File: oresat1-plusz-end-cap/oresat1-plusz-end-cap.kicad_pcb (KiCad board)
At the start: 4 copper layers, 105.6 x 105.6 mm, 48 parts, among them J1 M55-7011242R, J2 U.FL-R-SMA, U1 RM3100, U2 RM3100

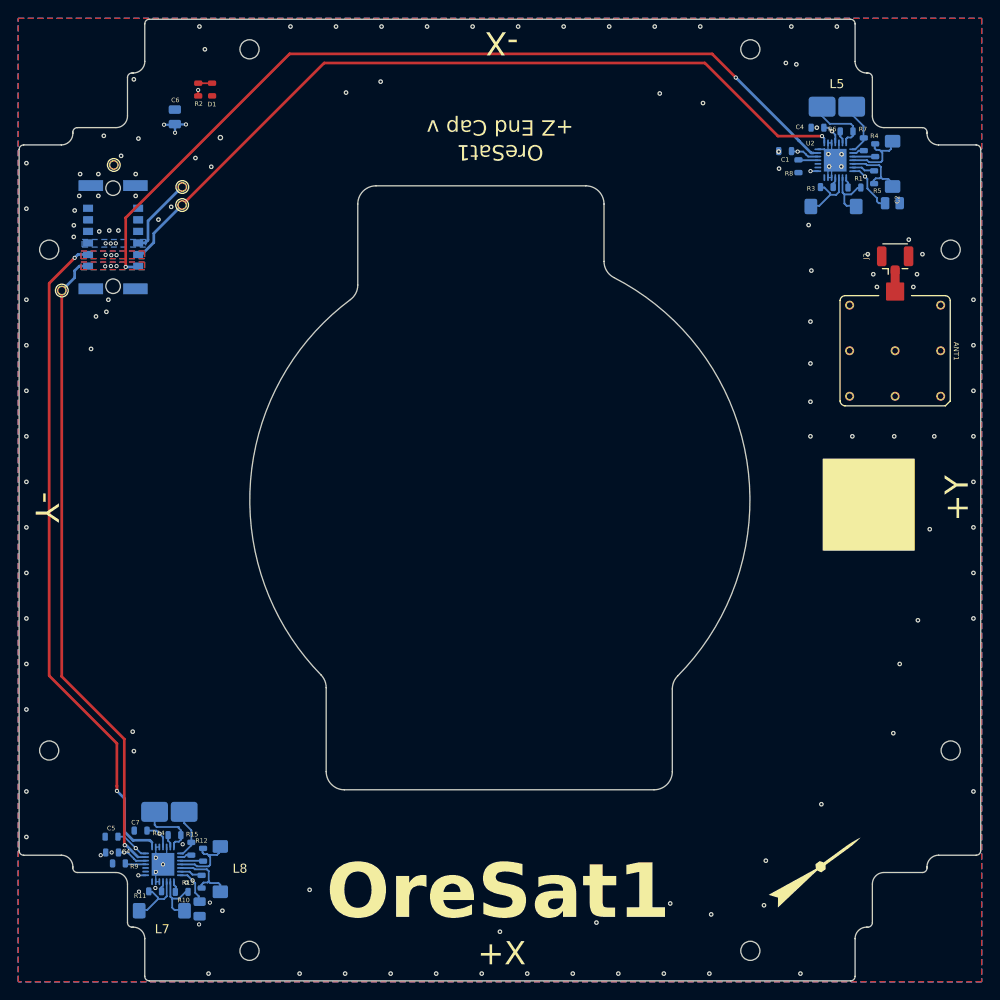
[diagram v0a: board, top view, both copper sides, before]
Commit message: Added 3D models and fixed fab des
3D models of antenna patch (-Z) and M55 connector & magIc2 chip on both boards.
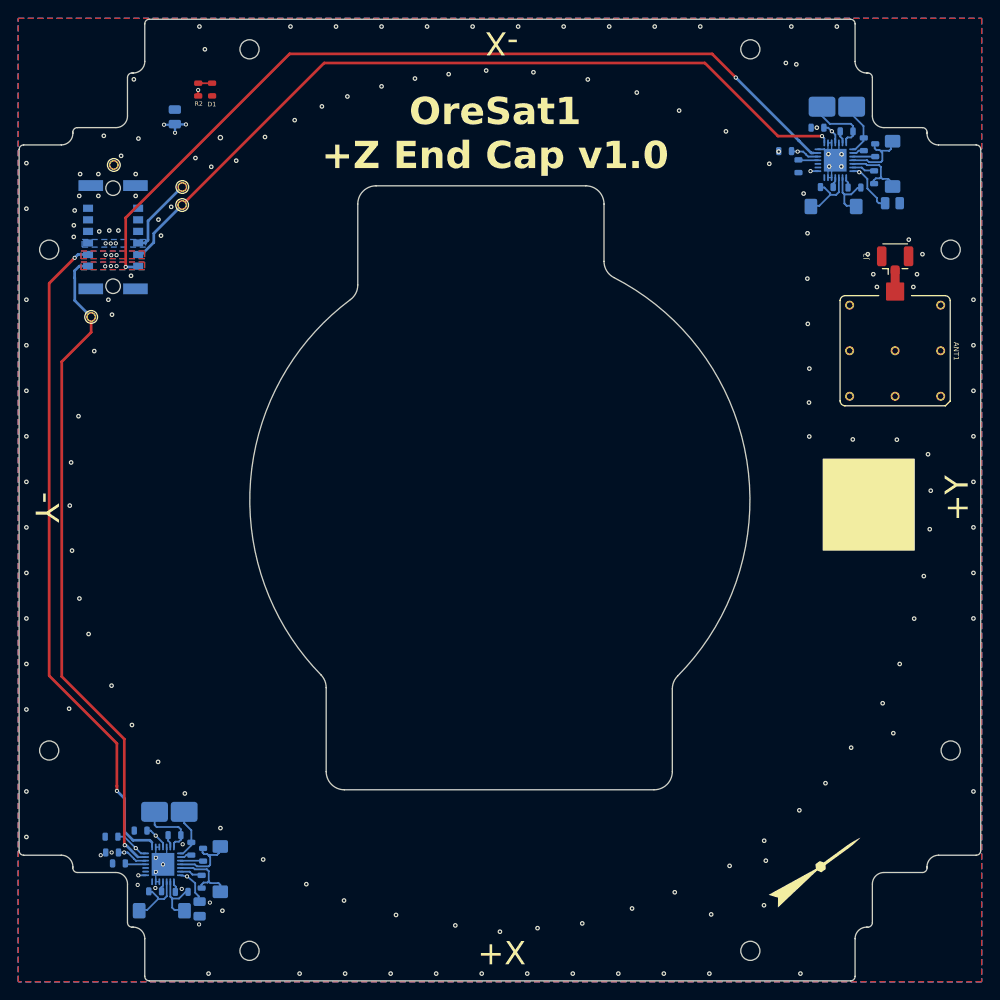
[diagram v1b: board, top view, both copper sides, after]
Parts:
- moved MAG-SDA 4.33 mm to (103.6, 84.9)
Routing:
- net /MAG-SDA: track 165.8 -> 167.3 mm
- net GND: vias 128 -> 163
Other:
- board text added: "OreSat1 +Z End Cap v1.0 ${ISSUE_DATE}"
- board text removed: "OreSat1"
- board text removed: "OreSat1 +Z End Cap v${REVISION}"

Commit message: +Z End Cap ready for fab and assembly.
Schematic: Made RM3100 symbol better, cleaned up schematic, added variable strings, DRC'd,
added fiducials

Layout: Added fiducials, cleaned up polygons, rerouted signals too close to the edge,
Fixed the connector to the +Z End Card (it was wrong in so many ways), added all the
3D models to things, fixed the Makefile to use STEP not VRML files, reset the footprint
libraries Added the correct and latest DXF outline. Removed old DXF and old crusty
3D and other footprint files. Most important: ADDED KAOMOJI.

Makefile: Added flag to output STEP file with STP models, not VRML.
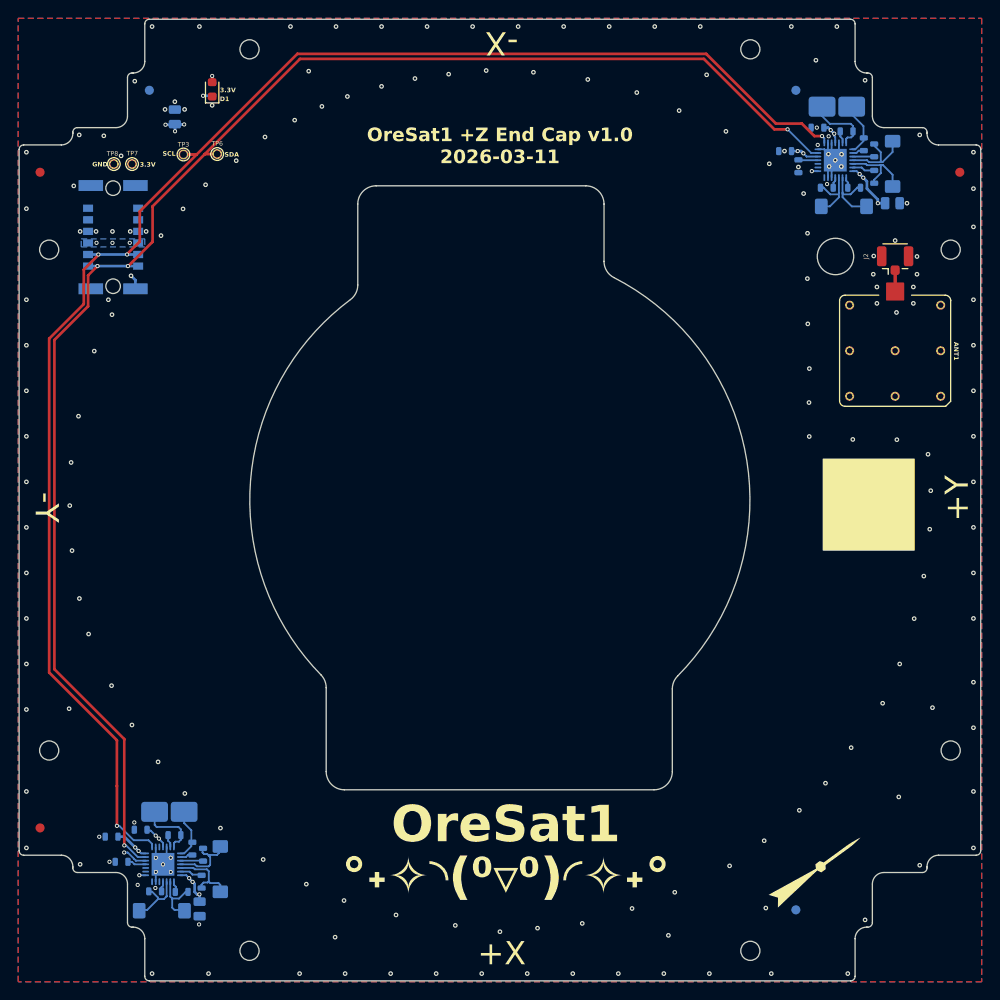
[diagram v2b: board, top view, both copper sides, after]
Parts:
- removed 3.3V, GND, MAG-SCL, MAG-SDA: Test-Point, oresat-misc:TestPoint-0.75mm-th
- removed the C4 at (105.9, 143.7)
- added FID101: Fiducial, Fiducial:Fiducial_1mm_Mask2mm, F.Cu at (98.0, 69.0)
- added FID102: Fiducial, Fiducial:Fiducial_1mm_Mask2mm, F.Cu at (199.0, 69.0)
- added FID103: Fiducial, Fiducial:Fiducial_1mm_Mask2mm, F.Cu at (98.0, 141.0)
- added FID104: Fiducial, Fiducial:Fiducial_1mm_Mask2mm, B.Cu at (181.0, 60.0)
- added FID105: Fiducial, Fiducial:Fiducial_1mm_Mask2mm, B.Cu at (110.0, 60.0)
- added FID106: Fiducial, Fiducial:Fiducial_1mm_Mask2mm, B.Cu at (181.0, 150.0)
- added REF**: MountingHole_4mm, MountingHole:MountingHole_4mm, F.Cu at (185.3, 78.2)
- added TP3: Test-Point, oresat-misc:TestPoint-0.75mm-th, F.Cu at (113.8, 67.0)
- added TP6: Test-Point, oresat-misc:TestPoint-0.75mm-th, F.Cu at (117.5, 67.0)
- added TP7: Test-Point, oresat-misc:TestPoint-0.75mm-th, F.Cu at (108.1, 68.1)
- added TP8: Test-Point, oresat-misc:TestPoint-0.75mm-th, F.Cu at (106.1, 68.1)
- D1: footprint oresat-passives:0603-C-NOSILK -> LED_SMD:LED_0603_1608Metric
- J1: footprint oresat0.5-plusz-end-cap:HARWIN-M55-70X1242R -> oresat-connectors:J-Harwin-M55-7XX1242R
- L3: value SEN2-XY (y-axis) -> RM3100-XY
- L4: value SEN2-XY (x-axis) -> RM3100-XY
- L5: value SEN2-Z (z-axis) -> RM3100-Z
- L7: value SEN1-XY (x-axis) -> RM3100-XY
- L8: value SEN1-XY (y-axis) -> RM3100-XY
- L9: value SEN1-Z (z-axis) -> RM3100-Z
- R2: moved to B.Cu
- moved R2 1.53 mm to (116.9, 59.9)
- moved L4 1.14 mm to (186.3, 72.8)
- moved R9 0.34 mm to (107.0, 144.7)
- moved R15 0.12 mm to (114.7, 143.3)
- moved R4 0.11 mm to (189.6, 66.6)
- moved C7 0.10 mm to (109.0, 141.2)
- moved R3 0.07 mm to (184.4, 70.7)
- moved R5 0.05 mm to (189.6, 69.5)
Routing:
- net /MAG-SCL: track 161.8 -> 172.0 mm, vias 6 -> 4
- net +3.3v: track 40.1 -> 30.2 mm, vias 16 -> 24
- net /MAG-SDA: track 167.3 -> 170.4 mm, vias 6 -> 4
- net GND: track 16.0 -> 18.2 mm, vias 163 -> 182
- net Net-(U2-XINP): track 6.31 -> 7.53 mm
- net Net-(U2-YINN): track 7.58 -> 8.47 mm
- net Net-(U2-YINP): track 7.73 -> 8.42 mm
- net Net-(D1-A): track 1.52 -> 1.46 mm, vias 0 -> 1
- net (no net): vias 1 -> 0
- removed copper zone on B.Cu, net /MAG-SCL
- removed copper zone on F.Cu, net /MAG-SCL
- removed copper zone on B.Cu, net /MAG-SDA
- removed copper zone on F.Cu, net /MAG-SDA
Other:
- board text added: "${TITLE} v${REVISION} ${ISSUE_DATE}"
- board text added: "3.3V"
- board text added: "GND"
- board text added: "OreSat1"
- board text added: "SCL"
- board text added: "SDA"
- board text added: "°˖✧◝(⁰▿⁰)◜✧˖°"
- board text removed: "OreSat1 +Z End Cap v1.0 ${ISSUE_DATE}"

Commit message: Added note on patch antenna
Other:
- board text added: "Backup S Band Patch Antenna"
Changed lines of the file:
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@@
+		)
+	)
+	(gr_text "Backup S Band Patch Antenna"
+		(at 186.375 95.7 0)
+		(layer "F.SilkS")
+		(effects
+			(font
+				(size 0.5 0.5)
+				(thickness 0.125)
+				(bold yes)
+			)
+			(justify left bottom)
 		)
 	)

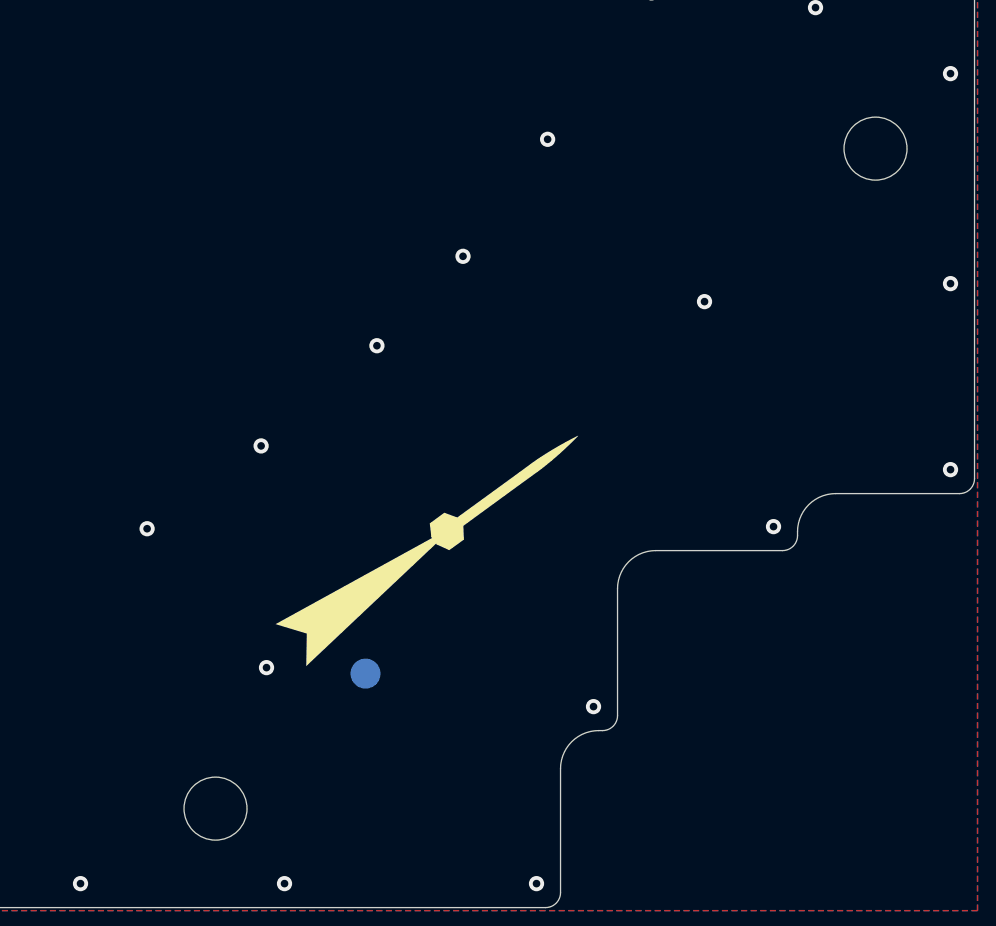
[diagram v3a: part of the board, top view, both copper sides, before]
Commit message: Added Oresat logo, updated PSAS logo!
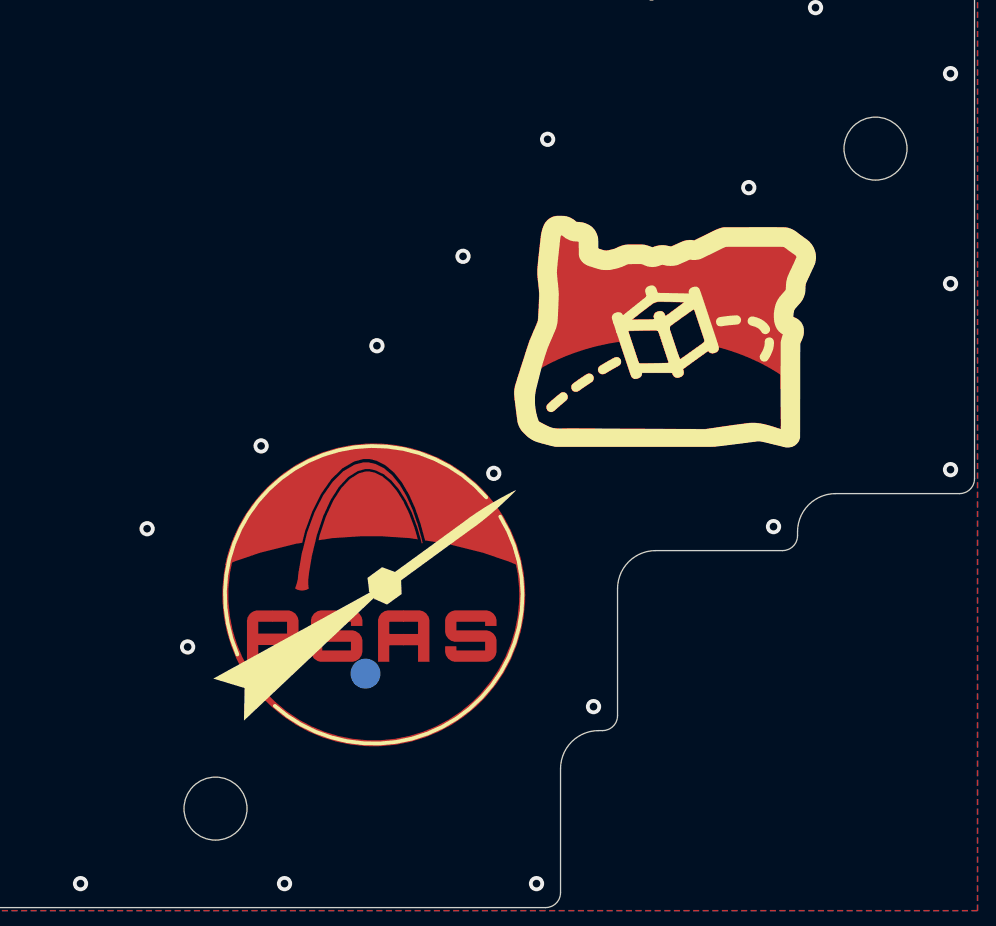
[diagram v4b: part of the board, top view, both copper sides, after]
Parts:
- added REF**: logo-small, oresat-graphics:logo-small, F.Cu at (190.9, 138.3)
- moved LOGO1 2.76 mm to (181.3, 147.4)
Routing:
- net GND: vias 182 -> 183
